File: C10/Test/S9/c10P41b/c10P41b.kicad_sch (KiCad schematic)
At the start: 6 parts

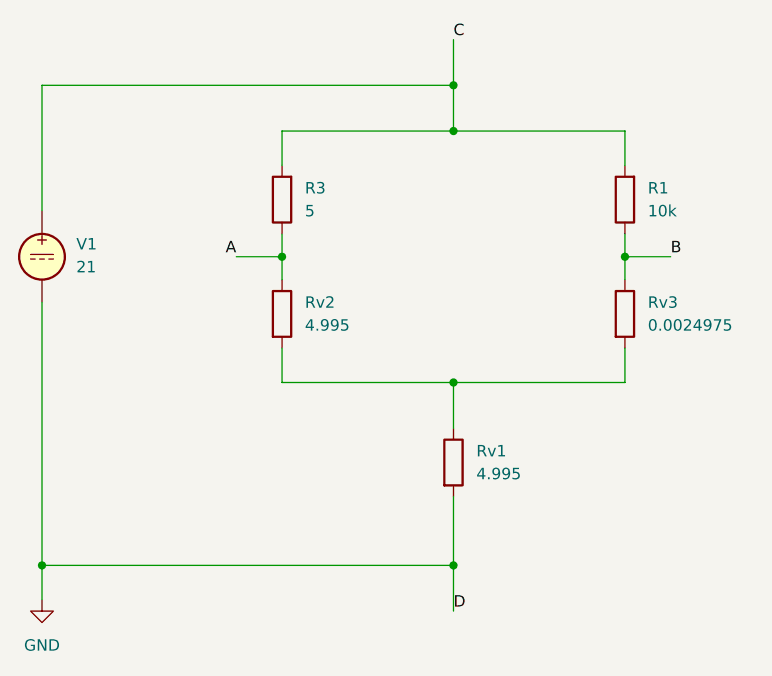
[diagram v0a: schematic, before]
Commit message: corrected due to misprinting Fig 10-45
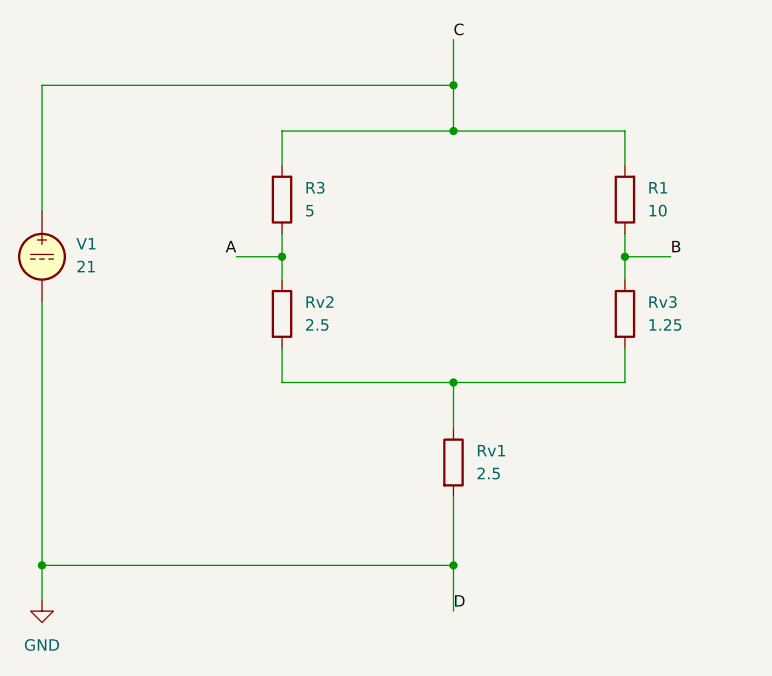
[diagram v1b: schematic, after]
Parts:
- R1: value 10k -> 10
- Rv1, Rv2: value 4.995 -> 2.5
- Rv3: value 0.0024975 -> 1.25
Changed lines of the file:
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@@
 			)
 		)
-		(property "Value" "0.0024975"
+		(property "Value" "1.25"
 			(at 176.53 90.1699 0)
 			(show_name no)
@@
 			)
 		)
-		(property "Value" "4.995"
+		(property "Value" "2.5"
 			(at 138.43 90.1699 0)
 			(show_name no)
@@
 			)
 		)
-		(property "Value" "10k"
+		(property "Value" "10"
 			(at 176.53 77.4699 0)
 			(show_name no)
@@
 			)
 		)
-		(property "Value" "4.995"
+		(property "Value" "2.5"
 			(at 157.48 106.6799 0)
 			(show_name no)
